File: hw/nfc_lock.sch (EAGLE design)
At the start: 8 parts, among them IC1 STM8S003F3, IC3 MCP170312MB, U1 M24SR16-YMN6T/2, X1 MINI-USB-32005-301

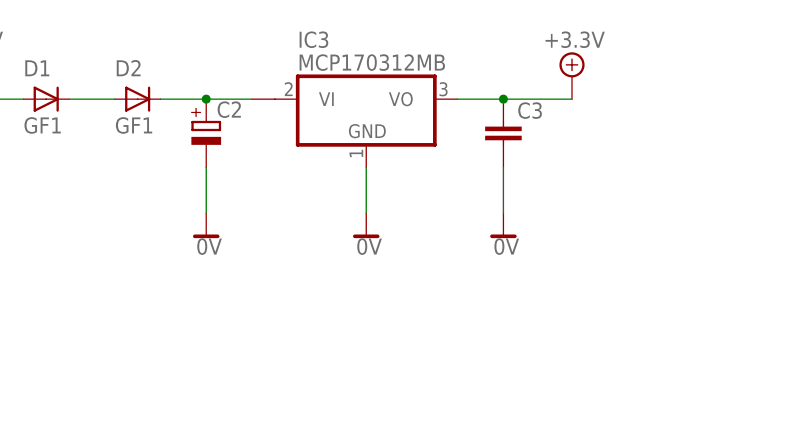
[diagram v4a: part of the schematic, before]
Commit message: added capacitors values
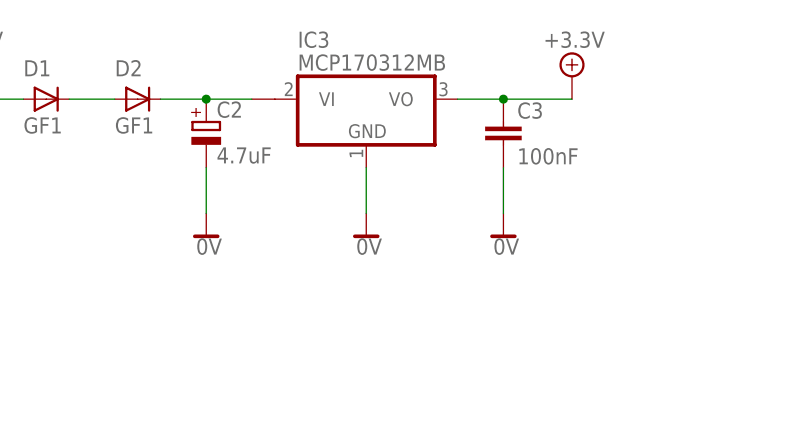
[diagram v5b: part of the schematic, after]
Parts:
- C2: value (none) -> 4.7uF
- C3: value (none) -> 100nF
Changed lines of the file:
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@@
 <layer number="48" name="Document" color="7" fill="1" visible="no" active="no"/>
 <layer number="49" name="Reference" color="7" fill="1" visible="no" active="no"/>
+<layer number="50" name="dxf" color="7" fill="1" visible="no" active="no"/>
 <layer number="51" name="tDocu" color="7" fill="1" visible="no" active="no"/>
 <layer number="52" name="bDocu" color="7" fill="1" visible="no" active="no"/>
+<layer number="53" name="tGND_GNDA" color="7" fill="9" visible="no" active="no"/>
+<layer number="54" name="bGND_GNDA" color="1" fill="9" visible="no" active="no"/>
+<layer number="56" name="wert" color="7" fill="1" visible="no" active="no"/>
+<layer number="57" name="tCAD" color="7" fill="1" visible="no" active="no"/>
+<layer number="59" name="tCarbon" color="7" fill="1" visible="no" active="no"/>
+<layer number="60" name="bCarbon" color="7" fill="1" visible="no" active="no"/>
 <layer number="90" name="Modules" color="5" fill="1" visible="yes" active="yes"/>
 <layer number="91" name="Nets" color="2" fill="1" visible="yes" active="yes"/>
@@
 <layer number="98" name="Guide" color="6" fill="1" visible="yes" active="yes"/>
 <layer number="99" name="SpiceOrder" color="5" fill="1" visible="yes" active="yes"/>
+<layer number="100" name="Muster" color="7" fill="1" visible="no" active="no"/>
+<layer number="101" name="Patch_Top" color="12" fill="4" visible="no" active="yes"/>
+<layer number="102" name="Vscore" color="7" fill="1" visible="no" active="yes"/>
+<layer number="103" name="fp3" color="7" fill="1" visible="no" active="yes"/>
+<layer number="104" name="Name" color="7" fill="1" visible="no" active="yes"/>
+<layer number="105" name="Beschreib" color="9" fill="1" visible="no" active="yes"/>
+<layer number="106" name="BGA-Top" color="4" fill="1" visible="no" active="yes"/>
+<layer number="107" name="BD-Top" color="5" fill="1" visible="no" active="yes"/>
+<layer number="108" name="fp8" color="7" fill="1" visible="no" active="yes"/>
+<layer number="109" name="fp9" color="7" fill="1" visible="no" active="yes"/>
+<layer number="110" name="fp0" color="7" fill="1" visible="no" active="yes"/>
+<layer number="111" name="LPC17xx" color="7" fill="1" visible="no" active="yes"/>
+<layer number="112" name="tSilk" color="7" fill="1" visible="no" active="yes"/>
+<layer number="113" name="ReferenceLS" color="7" fill="1" visible="no" active="no"/>
+<layer number="116" name="Patch_BOT" color="9" fill="4" visible="no" active="yes"/>
+<layer number="118" name="Rect_Pads" color="7" fill="1" visible="no" active="no"/>
+<layer number="121" name="_tsilk" color="7" fill="1" visible="no" active="yes"/>
+<layer number="122" name="_bsilk" color="7" fill="1" visible="no" active="yes"/>
+<layer number="123" name="tTestmark" color="7" fill="1" visible="no" active="yes"/>
+<layer number="124" name="bTestmark" color="7" fill="1" visible="no" active="yes"/>
+<layer number="125" name="_tNames" color="7" fill="1" visible="no" active="yes"/>
+<layer number="126" name="_bNames" color="7" fill="1" visible="no" active="yes"/>
+<layer number="127" name="_tValues" color="7" fill="1" visible="no" active="yes"/>
+<layer number="128" name="_bValues" color="7" fill="1" visible="no" active="yes"/>
+<layer number="129" name="Mask" color="7" fill="1" visible="yes" active="yes"/>
+<layer number="131" name="tAdjust" color="7" fill="1" visible="no" active="yes"/>
+<layer number="132" name="bAdjust" color="7" fill="1" visible="no" active="yes"/>
+<layer number="144" name="Drill_legend" color="7" fill="1" visible="no" active="yes"/>
+<layer number="150" name="Notes" color="7" fill="1" visible="no" active="yes"/>
+<layer number="151" name="HeatSink" color="7" fill="1" visible="no" active="yes"/>
+<layer number="152" name="_bDocu" color="7" fill="1" visible="no" active="yes"/>
+<layer number="153" name="FabDoc1" color="6" fill="1" visible="no" active="no"/>
+<layer number="154" name="FabDoc2" color="2" fill="1" visible="no" active="no"/>
+<layer number="155" name="FabDoc3" color="7" fill="15" visible="no" active="no"/>
+<layer number="199" name="Contour" color="7" fill="1" visible="no" active="yes"/>
+<layer number="200" name="200bmp" color="1" fill="10" visible="no" active="yes"/>
+<layer number="201" name="201bmp" color="2" fill="1" visible="no" active="no"/>
+<layer number="202" name="202bmp" color="3" fill="1" visible="no" active="no"/>
+<layer number="203" name="203bmp" color="4" fill="10" visible="no" active="yes"/>
+<layer number="204" name="204bmp" color="5" fill="10" visible="no" active="yes"/>
+<layer number="205" name="205bmp" color="6" fill="10" visible="no" active="yes"/>
+<layer number="206" name="206bmp" color="7" fill="10" visible="no" active="yes"/>
+<layer number="207" name="207bmp" color="8" fill="10" visible="no" active="yes"/>
+<layer number="208" name="208bmp" color="9" fill="10" visible="no" active="yes"/>
+<layer number="209" name="209bmp" color="7" fill="1" visible="no" active="yes"/>
+<layer number="210" name="210bmp" color="7" fill="1" visible="no" active="yes"/>
+<layer number="211" name="211bmp" color="7" fill="1" visible="no" active="yes"/>
+<layer number="212" name="212bmp" color="7" fill="1" visible="no" active="yes"/>
+<layer number="213" name="213bmp" color="7" fill="1" visible="no" active="yes"/>
+<layer number="214" name="214bmp" color="7" fill="1" visible="no" active="yes"/>
+<layer number="215" name="215bmp" color="7" fill="1" visible="no" active="yes"/>
+<layer number="216" name="216bmp" color="7" fill="1" visible="no" active="yes"/>
+<layer number="217" name="217bmp" color="18" fill="1" visible="no" active="no"/>
+<layer number="218" name="218bmp" color="19" fill="1" visible="no" active="no"/>
+<layer number="219" name="219bmp" color="20" fill="1" visible="no" active="no"/>
+<layer number="220" name="220bmp" color="21" fill="1" visible="no" active="no"/>
+<layer number="221" name="221bmp" color="22" fill="1" visible="no" active="no"/>
+<layer number="222" name="222bmp" color="23" fill="1" visible="no" active="no"/>
+<layer number="223" name="223bmp" color="24" fill="1" visible="no" active="no"/>
+<layer number="224" name="224bmp" color="25" fill="1" visible="no" active="no"/>
+<layer number="225" name="225bmp" color="7" fill="1" visible="yes" active="yes"/>
+<layer number="226" name="226bmp" color="7" fill="1" visible="yes" active="yes"/>
+<layer number="227" name="227bmp" color="7" fill="1" visible="yes" active="yes"/>
+<layer number="228" name="228bmp" color="7" fill="1" visible="yes" active="yes"/>
+<layer number="229" name="229bmp" color="7" fill="1" visible="yes" active="yes"/>
+<layer number="230" name="230bmp" color="7" fill="1" visible="yes" active="yes"/>
+<layer number="231" name="Eagle3D_PG1" color="7" fill="1" visible="no" active="no"/>
+<layer number="232" name="Eagle3D_PG2" color="7" fill="1" visible="no" active="no"/>
+<layer number="233" name="Eagle3D_PG3" color="7" fill="1" visible="no" active="no"/>
+<layer number="248" name="Housing" color="7" fill="1" visible="no" active="yes"/>
+<layer number="249" name="Edge" color="7" fill="1" visible="no" active="yes"/>
+<layer number="250" name="Descript" color="7" fill="1" visible="no" active="no"/>
+<layer number="251" name="SMDround" color="7" fill="1" visible="no" active="no"/>
+<layer number="254" name="cooling" color="7" fill="1" visible="no" active="yes"/>
+<layer number="255" name="routoute" color="7" fill="1" visible="yes" active="yes"/>
 </layers>
 <schematic xreflabel="%F%N/%S.%C%R" xrefpart="/%S.%C%R">
@@
 <part name="SUPPLY2" library="supply2" deviceset="+5V/1" device="" value="+3.3V"/>
 <part name="SUPPLY3" library="supply2" deviceset="0V" device=""/>
-<part name="C2" library="rcl" deviceset="CPOL-EU" device="153CLV-0405"/>
-<part name="C3" library="rcl" deviceset="C-EU" device="C1206"/>
+<part name="C2" library="rcl" deviceset="CPOL-EU" device="153CLV-0405" value="4.7uF"/>
+<part name="C3" library="rcl" deviceset="C-EU" device="C1206" value="100nF"/>
 <part name="D1" library="diode" deviceset="GF1" device=""/>
 <part name="D2" library="diode" deviceset="GF1" device=""/>

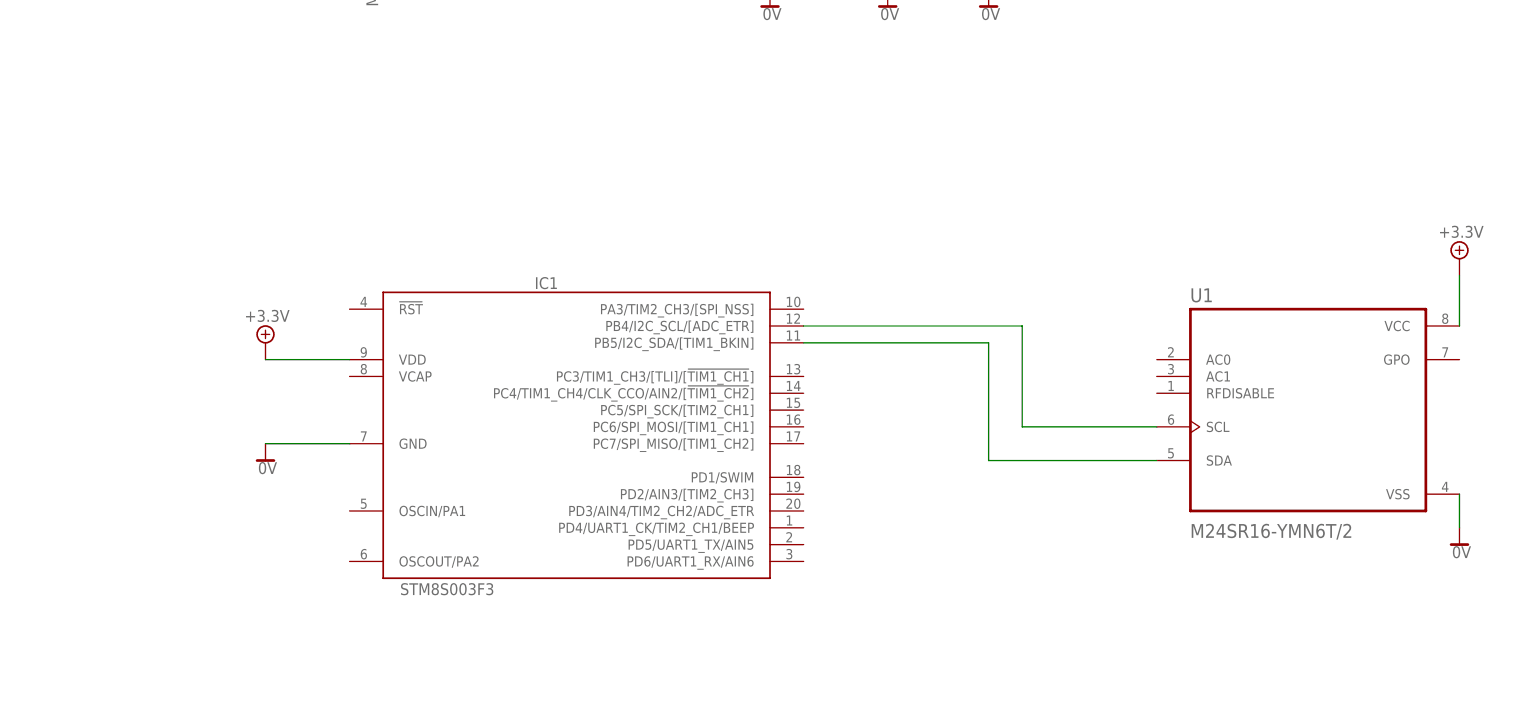
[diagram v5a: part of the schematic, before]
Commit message: added more lines and power n-mosfet to schema
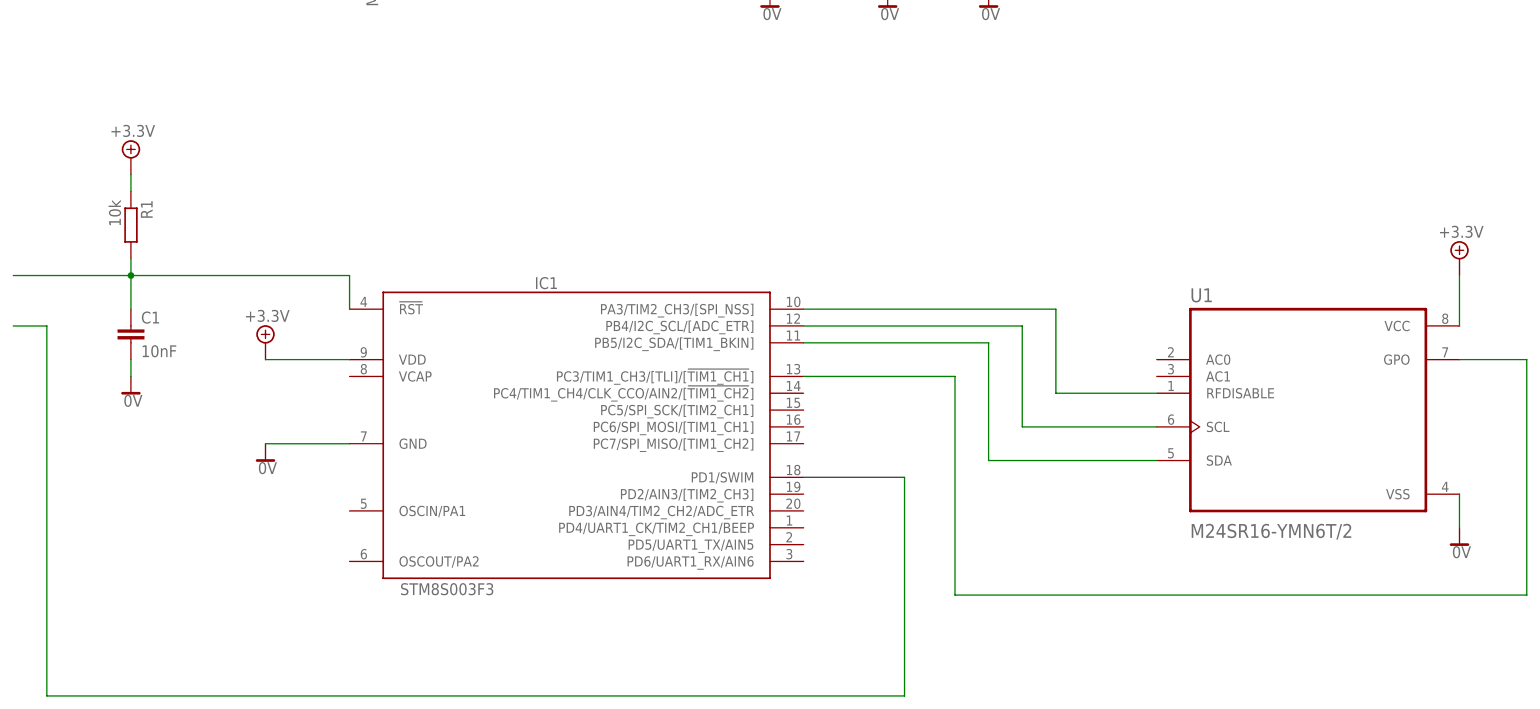
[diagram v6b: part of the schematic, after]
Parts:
- added C1: 10nF, rcl:C-EUC1206
- added R1: 10k, rcl:R-EU_R0805
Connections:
- new net N$5: C1.1, IC1.!RST, R1.2
- new net N$6: IC1.PD1/SWIM
- new net N$7: IC1.PA3/TIM2_CH3/[SPI_NSS], U1.RFDISABLE
- new net N$8: IC1.PC3/TIM1_CH3/[TLI]/[!TIM1_CH1!], U1.GPO
- net +5V/1: now also R1.1
- net 0V: now also C1.2
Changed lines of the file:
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@@
 <part name="SUPPLY10" library="supply2" deviceset="0V" device=""/>
 <part name="SUPPLY11" library="supply2" deviceset="+5V/1" device="" value="+3.3V"/>
+<part name="R1" library="rcl" deviceset="R-EU_" device="R0805" value="10k"/>
+<part name="C1" library="rcl" deviceset="C-EU" device="C1206" value="10nF"/>
+<part name="SUPPLY12" library="supply2" deviceset="+5V/1" device="" value="+3.3V"/>
+<part name="SUPPLY13" library="supply2" deviceset="0V" device=""/>
 </parts>
 <sheets>
@@
 <instance part="SUPPLY10" gate="0V" x="157.48" y="58.42"/>
 <instance part="SUPPLY11" gate="G$1" x="157.48" y="101.6"/>
+<instance part="R1" gate="G$1" x="-43.18" y="106.68" rot="R270"/>
+<instance part="C1" gate="G$1" x="-43.18" y="91.44"/>
+<instance part="SUPPLY12" gate="G$1" x="-43.18" y="116.84"/>
+<instance part="SUPPLY13" gate="0V" x="-43.18" y="81.28"/>
 </instances>
 <busses>
@@
 <wire x1="157.48" y1="60.96" x2="157.48" y2="66.04" width="0.1524" layer="91"/>
 </segment>
+<segment>
+<pinref part="C1" gate="G$1" pin="2"/>
+<pinref part="SUPPLY13" gate="0V" pin="0V"/>
+<wire x1="-43.18" y1="83.82" x2="-43.18" y2="86.36" width="0.1524" layer="91"/>
+</segment>
 </net>
 <net name="+5V/1" class="0">
@@
 <pinref part="SUPPLY11" gate="G$1" pin="+5V/1"/>
 <wire x1="157.48" y1="99.06" x2="157.48" y2="91.44" width="0.1524" layer="91"/>
+</segment>
+<segment>
+<pinref part="R1" gate="G$1" pin="1"/>
+<pinref part="SUPPLY12" gate="G$1" pin="+5V/1"/>
+<wire x1="-43.18" y1="114.3" x2="-43.18" y2="111.76" width="0.1524" layer="91"/>
 </segment>
 </net>
@@
 </segment>
 </net>
+<net name="N$5" class="0">
+<segment>
+<pinref part="C1" gate="G$1" pin="1"/>
+<pinref part="R1" gate="G$1" pin="2"/>
+<wire x1="-43.18" y1="101.6" x2="-43.18" y2="99.06" width="0.1524" layer="91"/>
+<pinref part="IC1" gate="G$1" pin="!RST"/>
+<wire x1="-43.18" y1="99.06" x2="-43.18" y2="93.98" width="0.1524" layer="91"/>
+<wire x1="-43.18" y1="99.06" x2="-10.16" y2="99.06" width="0.1524" layer="91"/>
+<wire x1="-10.16" y1="99.06" x2="-10.16" y2="93.98" width="0.1524" layer="91"/>
+<wire x1="-43.18" y1="99.06" x2="-60.96" y2="99.06" width="0.1524" layer="91"/>
+<junction x="-43.18" y="99.06"/>
+</segment>
+</net>
+<net name="N$6" class="0">
+<segment>
+<pinref part="IC1" gate="G$1" pin="PD1/SWIM"/>
+<wire x1="58.42" y1="68.58" x2="73.66" y2="68.58" width="0.1524" layer="91"/>
+<wire x1="73.66" y1="68.58" x2="73.66" y2="35.56" width="0.1524" layer="91"/>
+<wire x1="73.66" y1="35.56" x2="-55.88" y2="35.56" width="0.1524" layer="91"/>
+<wire x1="-55.88" y1="35.56" x2="-55.88" y2="91.44" width="0.1524" layer="91"/>
+<wire x1="-55.88" y1="91.44" x2="-60.96" y2="91.44" width="0.1524" layer="91"/>
+</segment>
+</net>
+<net name="N$7" class="0">
+<segment>
+<pinref part="IC1" gate="G$1" pin="PA3/TIM2_CH3/[SPI_NSS]"/>
+<wire x1="58.42" y1="93.98" x2="96.52" y2="93.98" width="0.1524" layer="91"/>
+<wire x1="96.52" y1="93.98" x2="96.52" y2="81.28" width="0.1524" layer="91"/>
+<pinref part="U1" gate="G$1" pin="RFDISABLE"/>
+<wire x1="96.52" y1="81.28" x2="111.76" y2="81.28" width="0.1524" layer="91"/>
+</segment>
+</net>
+<net name="N$8" class="0">
+<segment>
+<pinref part="IC1" gate="G$1" pin="PC3/TIM1_CH3/[TLI]/[!TIM1_CH1!]"/>
+<wire x1="58.42" y1="83.82" x2="81.28" y2="83.82" width="0.1524" layer="91"/>
+<wire x1="81.28" y1="83.82" x2="81.28" y2="50.8" width="0.1524" layer="91"/>
+<wire x1="81.28" y1="50.8" x2="167.64" y2="50.8" width="0.1524" layer="91"/>
+<wire x1="167.64" y1="50.8" x2="167.64" y2="86.36" width="0.1524" layer="91"/>
+<pinref part="U1" gate="G$1" pin="GPO"/>
+<wire x1="167.64" y1="86.36" x2="157.48" y2="86.36" width="0.1524" layer="91"/>
+</segment>
+</net>
